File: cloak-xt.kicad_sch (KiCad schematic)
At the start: 21 parts, among them J1 JST, U1 STM32F072CBT6

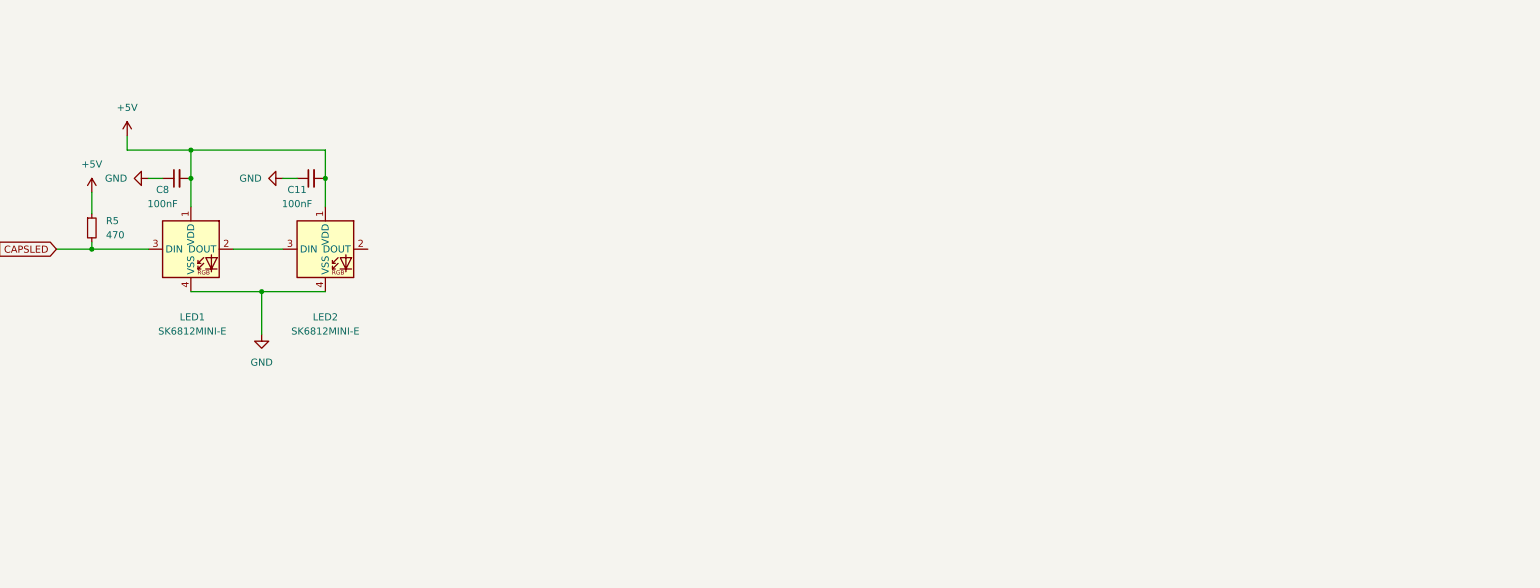
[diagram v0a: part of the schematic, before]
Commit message: Add schematics for RGB lighting
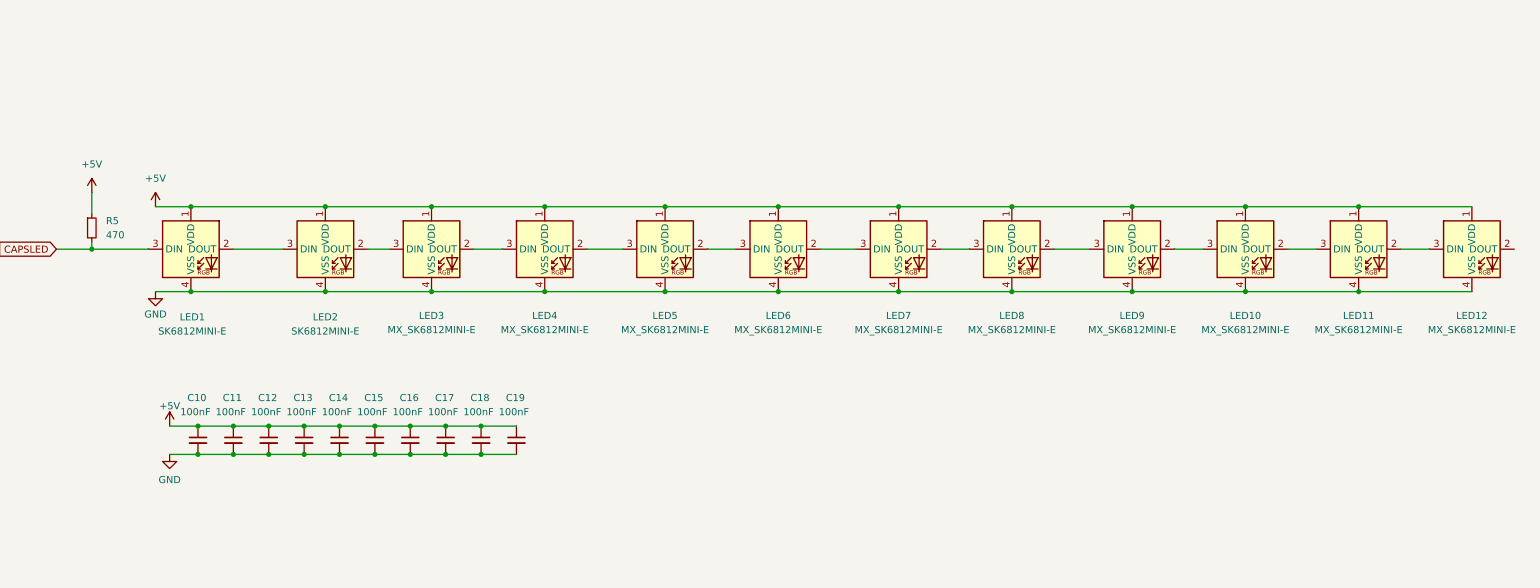
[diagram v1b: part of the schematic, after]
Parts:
- removed C8: 100nF, Capacitor_SMD:C_0402_1005Metric, symbol Device:C_Small
- added C10, C12, C13, C14, C15, C16, C17, C18, C19: 100nF, Capacitor_SMD:C_0402_1005Metric, symbol Device:C_Small
- added LED10, LED11, LED12, LED3, LED4, LED5, LED6, LED7, LED8, LED9: MX_SK6812MINI-E, PCM_marbastlib-mx:LED_MX_6028R-ROT, symbol PCM_marbastlib-mx:MX_SK6812MINI-E
- C11: LCSC (none) -> C1525
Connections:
- net +5V: now also C11.1, C10.1, C12.1, C13.1, C14.1, C15.1, C16.1, C17.1, C18.1, C19.1, LED10.1 (VDD), LED11.1 (VDD), LED12.1 (VDD), LED3.1 (VDD), LED4.1 (VDD), LED5.1 (VDD), LED6.1 (VDD), LED7.1 (VDD), LED8.1 (VDD), LED9.1 (VDD); no longer C11.2
- net GND: now also C11.2, C10.2, C12.2, C13.2, C14.2, C15.2, C16.2, C17.2, C18.2, C19.2, LED10.4 (VSS), LED11.4 (VSS), LED12.4 (VSS), LED3.4 (VSS), LED4.4 (VSS), LED5.4 (VSS), LED6.4 (VSS), LED7.4 (VSS), LED8.4 (VSS), LED9.4 (VSS); no longer C11.1
- net at LED2.2 (DOUT): now also LED3.3 (DIN)
- new net: LED5.2 (DOUT), LED6.3 (DIN)
- new net: LED4.2 (DOUT), LED5.3 (DIN)
- new net: LED8.2 (DOUT), LED9.3 (DIN)
- new net: LED7.2 (DOUT), LED8.3 (DIN)
- new net: LED6.2 (DOUT), LED7.3 (DIN)
- new net: LED3.2 (DOUT), LED4.3 (DIN)
- new net: LED10.2 (DOUT), LED11.3 (DIN)
- new net: LED10.3 (DIN), LED9.2 (DOUT)
- new net: LED11.2 (DOUT), LED12.3 (DIN)

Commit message: Initiate files for JLCPCB
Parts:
- removed C10: 100nF, Capacitor_SMD:C_0402_1005Metric, symbol Device:C_Small
- added C20, C21, C8: 100nF, Capacitor_SMD:C_0402_1005Metric, symbol Device:C_Small
- C11, C12, C13, C14, C15, C16, C17, C18, C19: LCSC C1525 -> (none)
- LED11: footprint PCM_marbastlib-mx:LED_MX_6028R-ROT -> PCM_marbastlib-mx:LED_MX_6028R
- R5: value 470 -> 4.7k
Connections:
- net A8 is gone; now on net COL0: U1.29 (PA8)
- net B0 is gone; now on net LED: U1.18 (PB0)
- net +5V: now also C11.2, C12.2, C13.2, C14.2, C15.2, C16.2, C17.2, C18.2, C19.2, C20.2, C21.2, C8.2; no longer C11.1, C12.1, C13.1, C14.1, C15.1, C16.1, C17.1, C18.1, C19.1
- net COL0: no longer U1.28 (PB15)
- net COL1: now also U1.28 (PB15); no longer U1.27 (PB14)
- net COL2: now also U1.27 (PB14); no longer U1.26 (PB13)
- net COL3: now also U1.26 (PB13); no longer U1.25 (PB12)
- net COL4: now also U1.22 (PB11); no longer U1.21 (PB10)
- net GND: now also C11.1, C12.1, C13.1, C14.1, C15.1, C16.1, C17.1, C18.1, C19.1, C20.1, C21.1, C8.1; no longer C11.2, C12.2, C13.2, C14.2, C15.2, C16.2, C17.2, C18.2, C19.2
- net ROW1: now also U1.25 (PB12); no longer U1.22 (PB11)
- net at LED5.2 (DOUT): now also LED4.3 (DIN); no longer LED6.3 (DIN)
- net at LED5.3 (DIN): now also LED6.2 (DOUT); no longer LED4.2 (DOUT)
- net at LED8.2 (DOUT): now also LED7.3 (DIN); no longer LED9.3 (DIN)
- net at LED8.3 (DIN): now also LED9.2 (DOUT); no longer LED7.2 (DOUT)
- net at LED3.2 (DOUT): now also LED2.3 (DIN); no longer LED4.3 (DIN)
- net at LED10.2 (DOUT): now also LED9.3 (DIN); no longer LED11.3 (DIN)
- net at LED10.3 (DIN): now also LED11.2 (DOUT); no longer LED9.2 (DOUT)
- net at LED3.3 (DIN): now also LED4.2 (DOUT); no longer LED2.2 (DOUT)
- net at LED1.2 (DOUT): no longer LED2.3 (DIN)
- net LED: now reaches LED12.3 (DIN)
- net LED: now also R5.2; no longer LED11.2 (DOUT)
- net at LED12.2 (DOUT): now also LED11.3 (DIN)
- net CAPSLED: no longer names the net of LED1.3 (DIN)
- net CAPSLED: now also LED2.2 (DOUT); no longer R5.2
- new net: LED6.3 (DIN), LED7.2 (DOUT)
- new net B10: U1.21 (PB10)
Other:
- moved on the sheet: R5

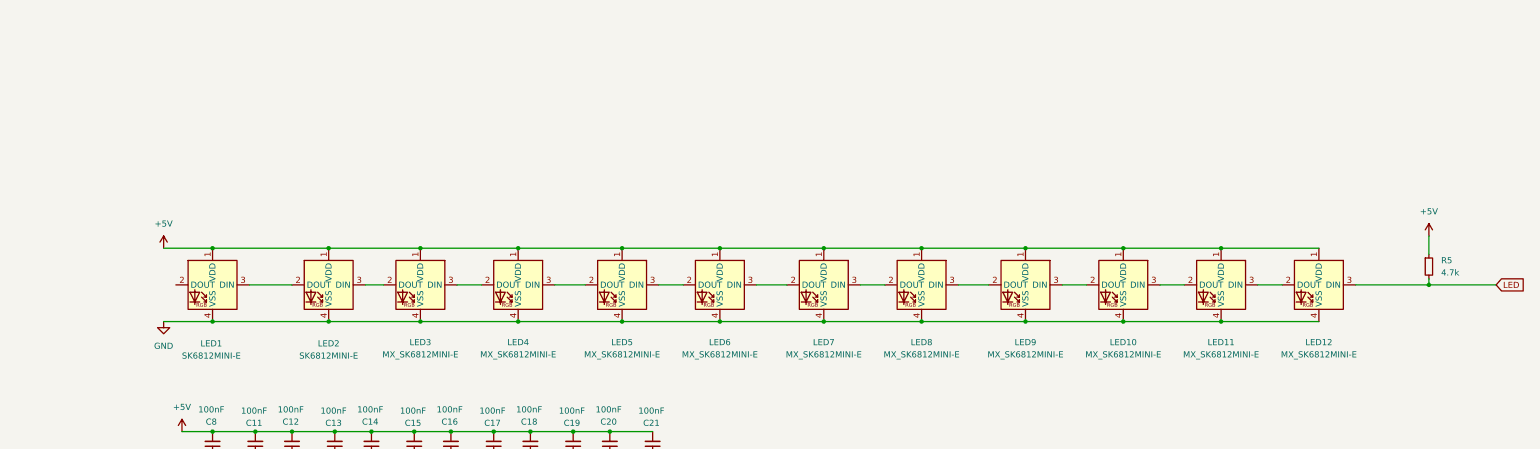
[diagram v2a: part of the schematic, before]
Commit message: Complete SK6812 LED traces
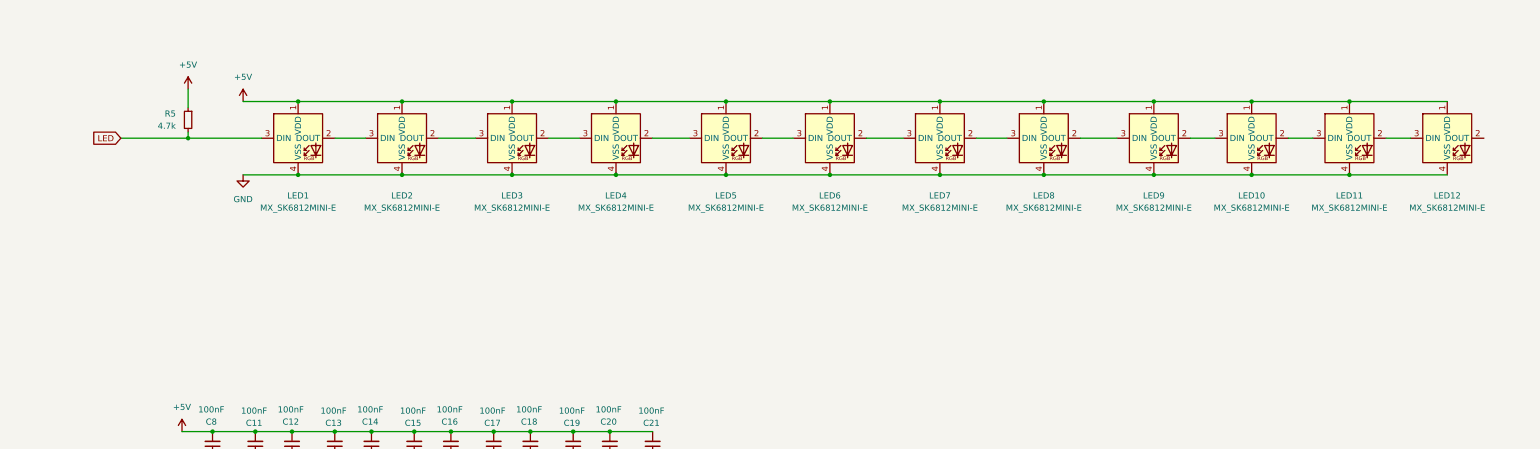
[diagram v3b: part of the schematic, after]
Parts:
- removed LED1, LED2: SK6812MINI-E, PCM_marbastlib-various:LED_6028R, symbol PCM_marbastlib-various:SK6812MINI-E
- added LED11, LED12: MX_SK6812MINI-E, PCM_marbastlib-various:LED_6028R, symbol PCM_marbastlib-mx:MX_SK6812MINI-E
- LED10, LED3, LED4, LED5, LED6, LED7, LED8, LED9: footprint PCM_marbastlib-mx:LED_MX_6028R-ROT -> PCM_marbastlib-mx:LED_MX_6028R
- renumbered LED12 to LED1, LED11 to LED2
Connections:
- net +5V: now also LED11.1 (VDD), LED12.1 (VDD)
- net GND: now also LED11.4 (VSS), LED12.4 (VSS)
- net at LED4.3 (DIN): now also LED3.2 (DOUT); no longer LED5.2 (DOUT)
- net at LED5.3 (DIN): now also LED4.2 (DOUT); no longer LED6.2 (DOUT)
- net at LED8.2 (DOUT): now also LED9.3 (DIN); no longer LED7.3 (DIN)
- net at LED9.2 (DOUT): now also LED10.3 (DIN); no longer LED8.3 (DIN)
- net at LED6.3 (DIN): now also LED5.2 (DOUT); no longer LED7.2 (DOUT)
- net at LED3.3 (DIN): now also LED2.2 (DOUT); no longer LED4.2 (DOUT)
- net at LED10.2 (DOUT): now also LED11.3 (DIN); no longer LED9.3 (DIN)
- new net: LED6.2 (DOUT), LED7.3 (DIN)
- new net: LED7.2 (DOUT), LED8.3 (DIN)
- new net: LED11.2 (DOUT), LED12.3 (DIN)
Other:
- moved on the sheet: LED1, LED2, R5

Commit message: Fixed and ignore silkscreen clipping
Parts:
- LED1: footprint PCM_marbastlib-mx:LED_MX_6028R-ROT -> PCM_marbastlib-mx:LED_MX_6028R
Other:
- note added: "JST Port"
- note added: "LED"
- note added: "MCU"
- note removed: "JST Port 5.1k resistors to GND on both CC pins will be on daughterboard and its indicate that this device is acting in legacy 2.0 UFP mode."
- moved on the sheet: BOOT1, C11, C12, C13, C14, C15, C16, C17, C18, C19, C20, C21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

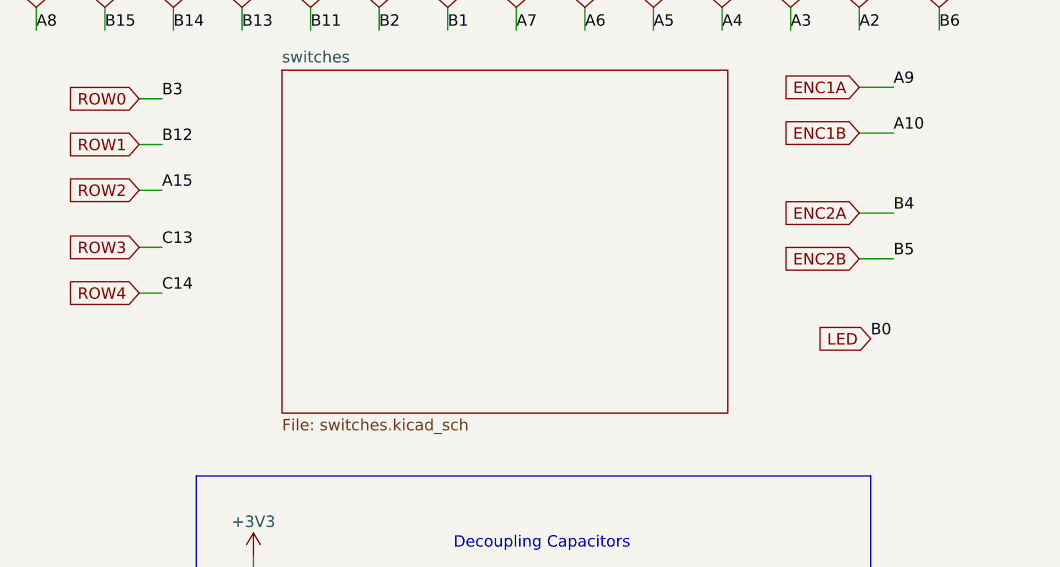
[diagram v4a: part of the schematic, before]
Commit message: Fix PF/PC pins and change LED pin to B8
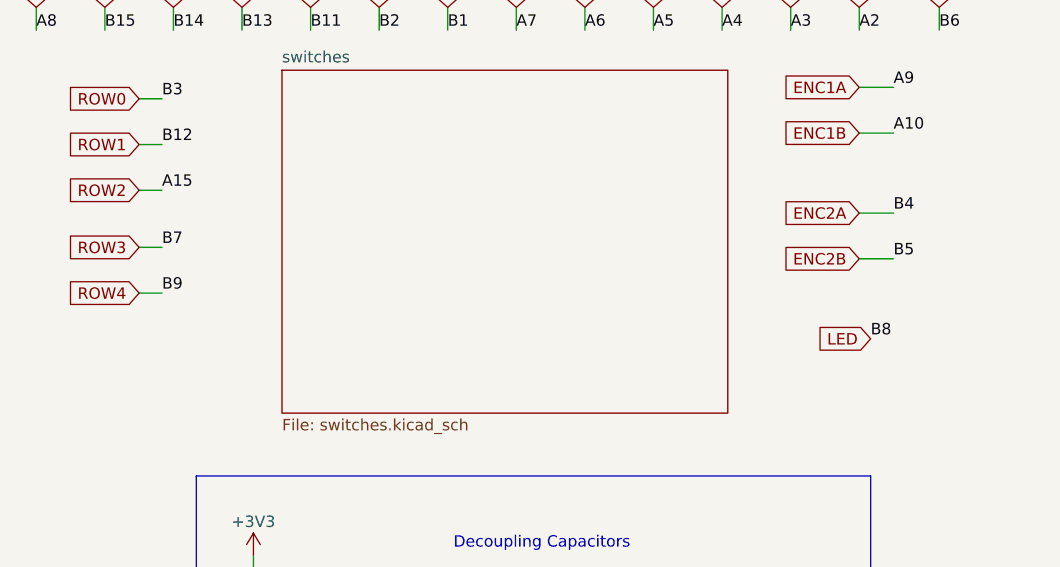
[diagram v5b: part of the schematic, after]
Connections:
- net B7 is gone; now on net ROW3: U1.43 (PB7)
- net B8 is gone; now on net LED: U1.45 (PB8)
- net B9 is gone; now on net ROW4: U1.46 (PB9)
- net LED: no longer U1.18 (PB0)
- net ROW3: no longer U1.2 (PC13)
- net ROW4: no longer U1.3 (PC14)
- new net B0: U1.18 (PB0)
- new net C13: U1.2 (PC13)
- new net C14: U1.3 (PC14)
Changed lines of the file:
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@@
-		)
-	)
-	(label "C13"
-		(at 177.8 59.69 0)
-		(fields_autoplaced yes)
-		(effects
-			(font
-				(size 1.27 1.27)
-			)
-			(justify left bottom)
 		)
 	)
@@
 		)
 	)
-	(label "C14"
-		(at 177.8 64.77 0)
-		(fields_autoplaced yes)
-		(effects
-			(font
-				(size 1.27 1.27)
-			)
-			(justify left bottom)
-		)
-	)
 	(label "B4"
 		(at 60.96 68.58 180)
@@
 		)
 	)
+	(label "B7"
+		(at 177.8 59.69 0)
+		(fields_autoplaced yes)
+		(effects
+			(font
+				(size 1.27 1.27)
+			)
+			(justify left bottom)
+		)
+	)
 	(label "A10"
 		(at 259.08 46.99 0)
@@
 		)
 	)
+	(label "B8"
+		(at 256.54 69.85 0)
+		(fields_autoplaced yes)
+		(effects
+			(font
+				(size 1.27 1.27)
+			)
+			(justify left bottom)
+		)
+	)
 	(label "C15"
 		(at 60.325 53.34 180)
@@
 		)
 	)
-	(label "B0"
-		(at 256.54 69.85 0)
-		(fields_autoplaced yes)
-		(effects
-			(font
-				(size 1.27 1.27)
-			)
-			(justify left bottom)
-		)
-	)
 	(label "B13"
 		(at 186.69 35.56 0)
 		(fields_autoplaced yes)
 		(effects
+			(font
+				(size 1.27 1.27)
+			)
+			(justify left bottom)
+		)
+	)
+	(label "B9"
+		(at 177.8 64.77 0)
+		(fields_autoplaced yes)
+		(effects

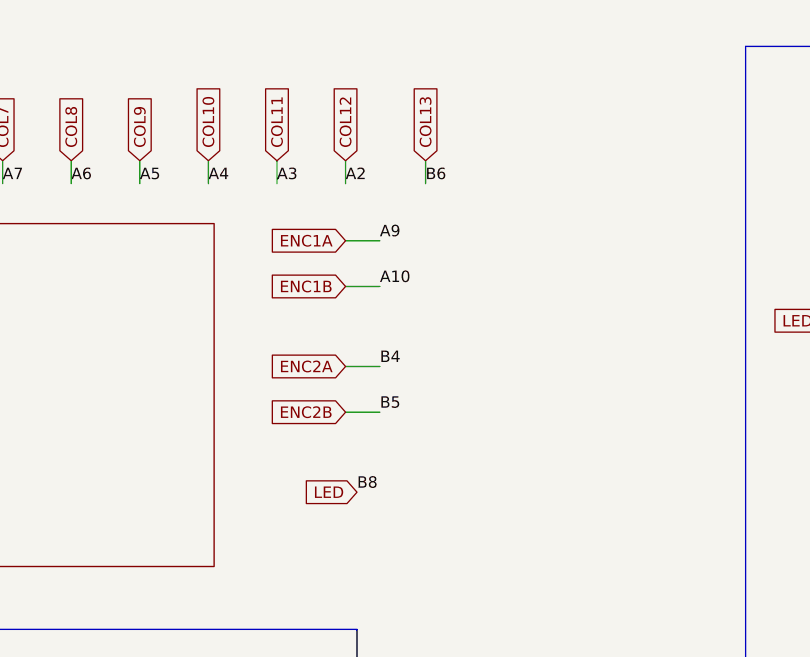
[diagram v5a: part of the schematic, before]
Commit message: Swap LED pin with ENC2B for TIM3_CH2
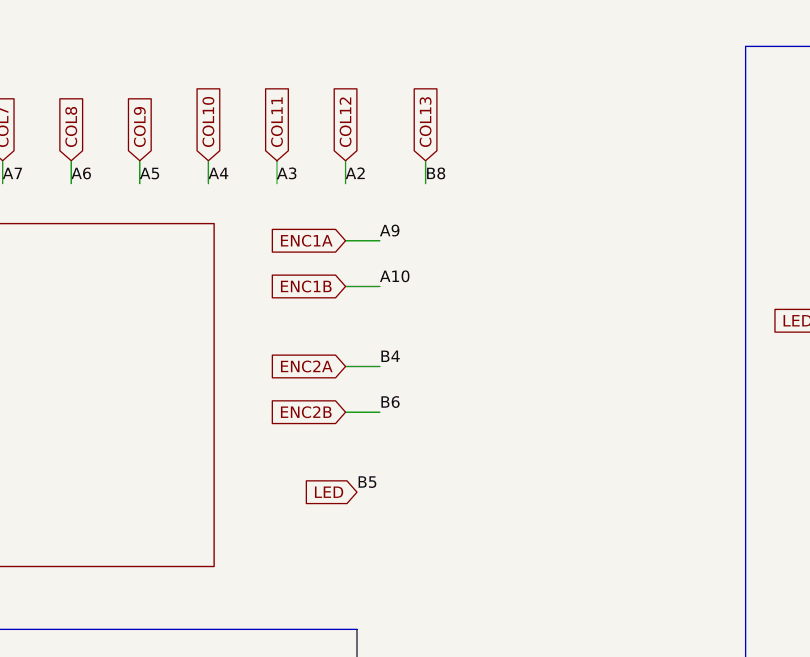
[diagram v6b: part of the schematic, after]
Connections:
- net COL13: now also U1.45 (PB8); no longer U1.42 (PB6)
- net ENC2B: now also U1.42 (PB6); no longer U1.41 (PB5)
- net LED: now also U1.41 (PB5); no longer U1.45 (PB8)
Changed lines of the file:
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@@
 	)
 	(label "B6"
-		(at 264.16 35.56 0)
+		(at 259.08 60.96 0)
 		(fields_autoplaced yes)
 		(effects
@@
 	)
 	(label "B8"
-		(at 256.54 69.85 0)
+		(at 264.16 35.56 0)
 		(fields_autoplaced yes)
 		(effects
@@
 	)
 	(label "B5"
-		(at 259.08 60.96 0)
+		(at 256.54 69.85 0)
 		(fields_autoplaced yes)
 		(effects

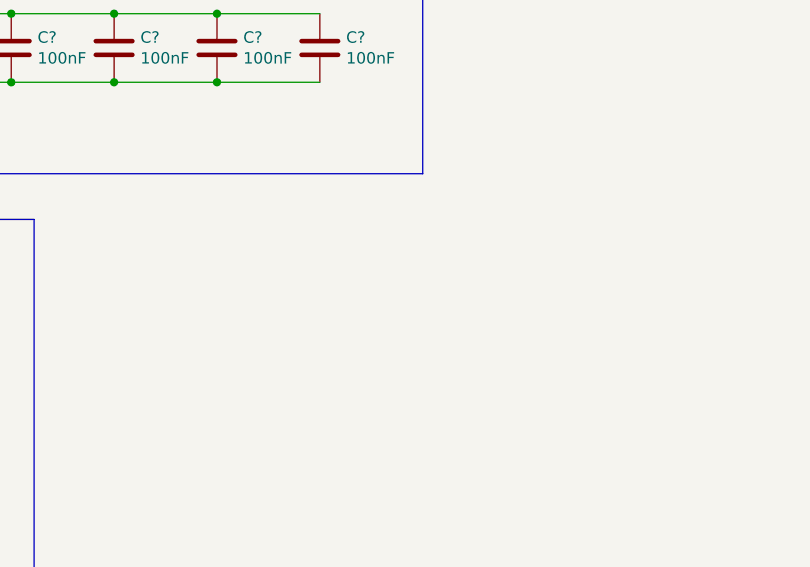
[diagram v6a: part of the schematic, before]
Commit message: Add pin for SW Debug
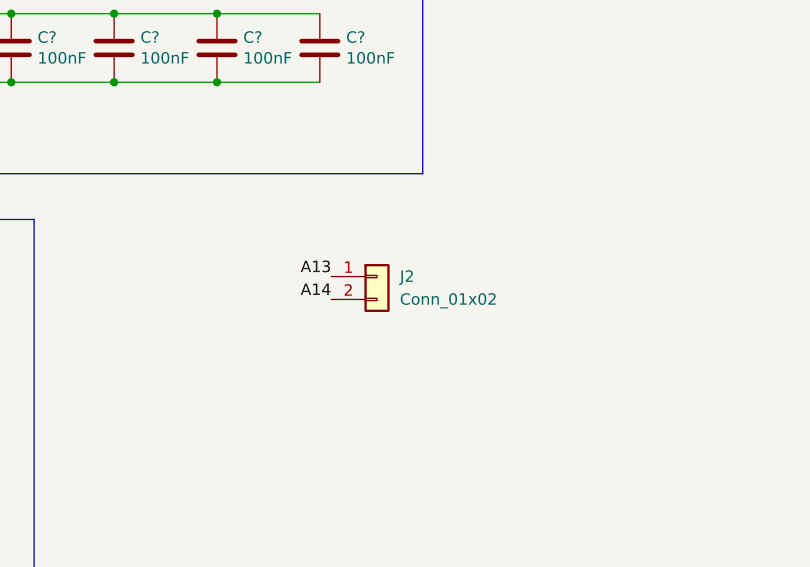
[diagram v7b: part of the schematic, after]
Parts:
- added J2: Conn_01x02, Connector_PinHeader_1.00mm:PinHeader_1x02_P1.00mm_Vertical, symbol Connector_Generic:Conn_01x02
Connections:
- net A13: now also J2.1 (Pin_1)
- net A14: now also J2.2 (Pin_2)
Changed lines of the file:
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@@
 		)
 	)
+	(label "A13"
+		(at 246.38 125.73 180)
+		(fields_autoplaced yes)
+		(effects
+			(font
+				(size 1.27 1.27)
+			)
+			(justify right bottom)
+		)
+	)
 	(label "B15"
 		(at 60.96 96.52 180)
@@
 		)
 	)
+	(label "A14"
+		(at 246.38 128.27 180)
+		(fields_autoplaced yes)
+		(effects
+			(font
+				(size 1.27 1.27)
+			)
+			(justify right bottom)
+		)
+	)
 	(label "C15"
 		(at 60.325 53.34 180)
@@
 					(unit 1)
 				)
+			)
+		)
+	)
+	(symbol
+		(lib_id "Connector_Generic:Conn_01x02")
+		(at 251.46 125.73 0)
+		(unit 1)
+		(exclude_from_sim no)
+		(in_bom yes)
+		(on_board yes)
+		(dnp no)
+		(fields_autoplaced yes)
+		(property "Reference" "J2"
+			(at 254 125.7299 0)
+			(effects
+				(font
+					(size 1.27 1.27)
+				)
+				(justify left)
+			)
+		)
+		(property "Value" "Conn_01x02"
+			(at 254 128.2699 0)
+			(effects
+				(font
+					(size 1.27 1.27)
+				)
+				(justify left)
+			)
+		)
+		(property "Footprint" "Connector_PinHeader_1.00mm:PinHeader_1x02_P1.00mm_Vertical"
+			(at 251.46 125.73 0)
+			(effects
+				(font
+					(size 1.27 1.27)
+				)
+				(hide yes)
+			)
+		)
+		(property "Datasheet" "~"
+			(at 251.46 125.73 0)
+			(effects
+				(font
+					(size 1.27 1.27)
+				)
+				(hide yes)
+			)
+		)
+		(property "Description" "Generic connector, single row, 01x02, script generated (kicad-library-utils/schlib/autogen/connector/)"
+			(at 251.46 125.73 0)
+			(effects
+				(font
+					(size 1.27 1.27)
+				)
+				(hide yes)
+			)
+		)
+		(pin "2"
+		)
+		(pin "1"
+		)
+		(instances
+			(project ""
+				(path "/4d291fcf-fdf2-46ba-aa57-60bc75f9cc32"
+					(reference "J2")
+					(unit 1)
+				)
